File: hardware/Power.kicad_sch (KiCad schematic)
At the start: 36 parts

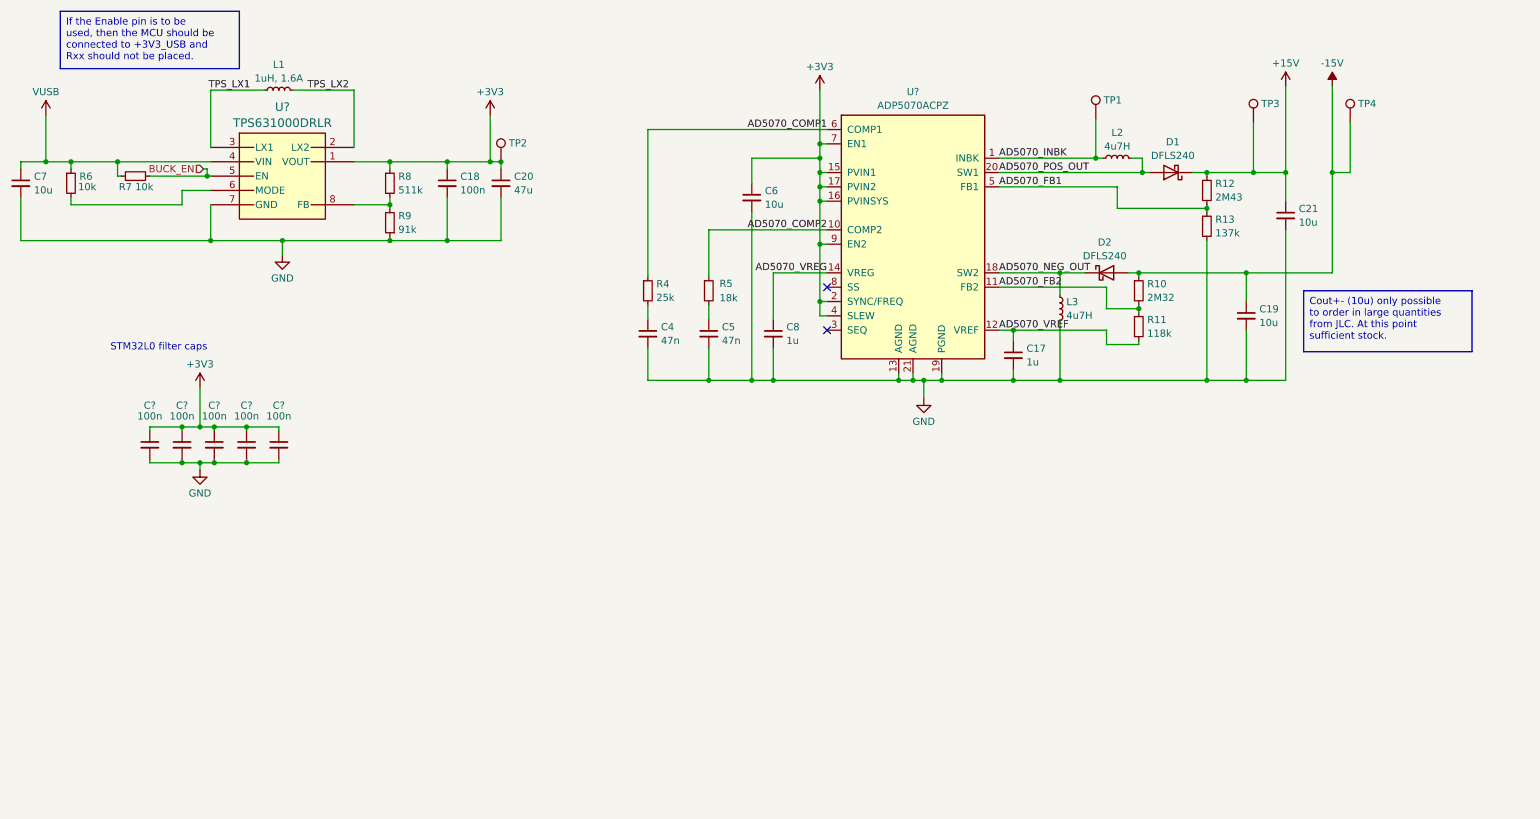
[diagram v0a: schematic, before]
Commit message: feat(RGB): WS2812B driver
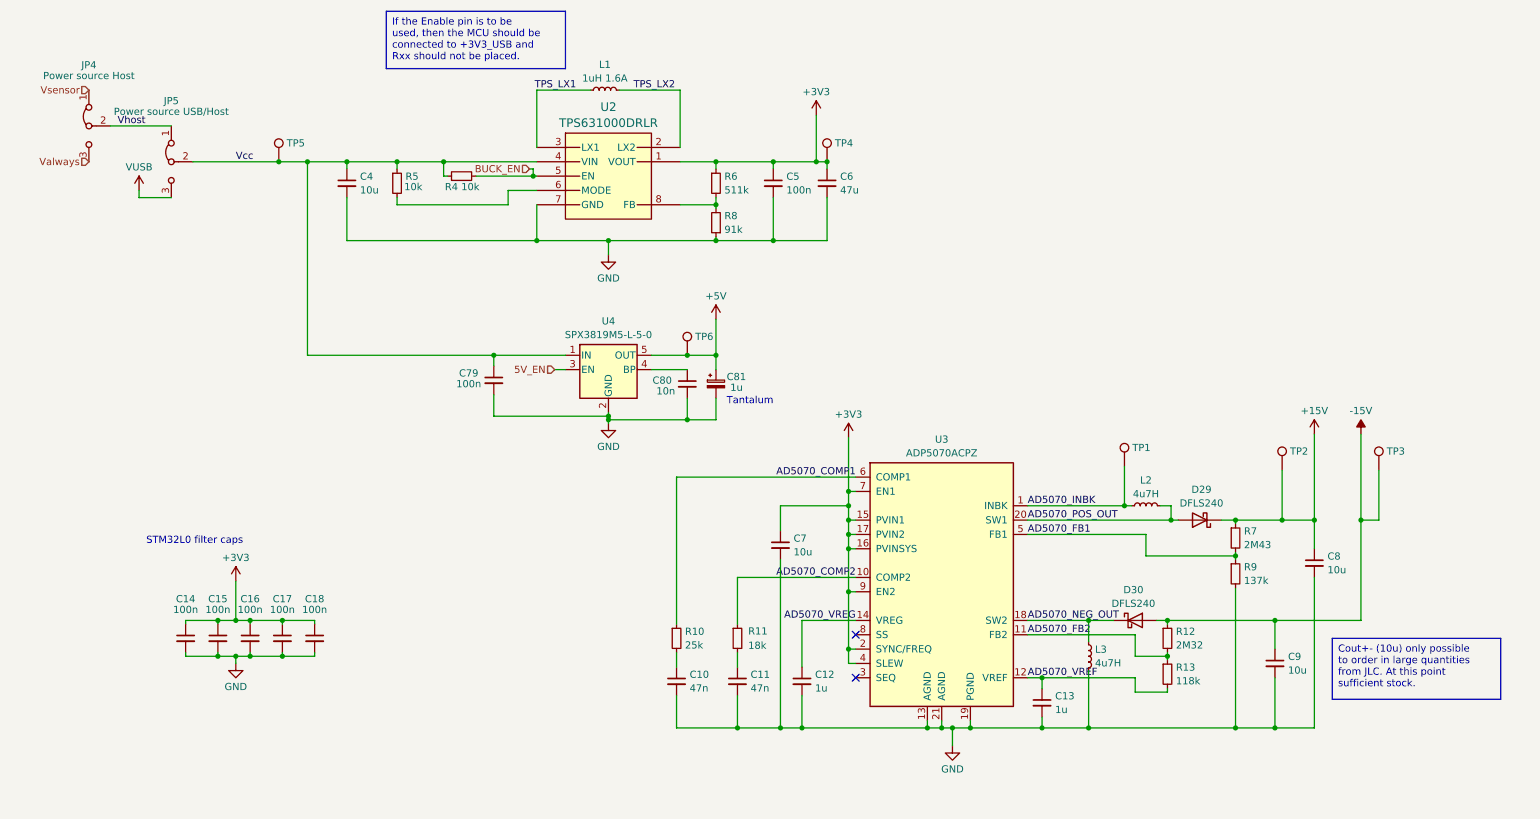
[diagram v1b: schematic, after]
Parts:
- added C79: 100n, Capacitor_SMD:C_0603_1608Metric, symbol Device:C_Small
- added C80: 10n, Capacitor_SMD:C_0603_1608Metric, symbol Device:C_Small
- added C81: 1u, Capacitor_Tantalum_SMD:CP_EIA-1608-08_AVX-J, symbol Device:C_Polarized_Small
- added JP4: Power source Host, Connector_PinHeader_2.54mm:PinHeader_1x03_P2.54mm_Vertical, symbol Jumper:Jumper_3_Bridged12
- added JP5: Power source USB/Host, Connector_PinHeader_2.54mm:PinHeader_1x03_P2.54mm_Vertical, symbol Jumper:Jumper_3_Bridged12
- added TP5, TP6: ~, TestPoint:TestPoint_Pad_D1.5mm, symbol Connector:TestPoint
- added U4: SPX3819M5-L-5-0, Package_TO_SOT_SMD:SOT-23-5, symbol Regulator_Linear:SPX3819M5-L-5-0
- L1: value 1uH, 1.6A -> 1uH 1.6A
- L2, L3: LCSC Part # (none) -> C9900037470
- gave numbers to parts that had none: 7
- renumbered C4 to C10, C5 to C11, C8 to C12, C17 to C13, C7 to C4, C18 to C5, C20 to C6, C6 to C7, C21 to C8, C19 to C9, D1 to D29, D2 to D30, R4 to R10, R5 to R11, R10 to R12, R11 to R13, R7 to R4, R6 to R5, R8 to R6, R12 to R7, R9 to R8, R13 to R9, TP3 to TP2, TP4 to TP3, TP2 to TP4
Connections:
- net GND: now also C79.2, C80.2, C81.2, U4.2 (GND)
- net VUSB: now also JP5.3 (B); no longer C4.1, R4.1, R5.1, U2.4 (VIN)
- new net: C80.1, U4.4 (BP)
- new net +5V: C81.1, TP6.1, U4.5 (OUT)
- new net 5V_EN: U4.3 (EN)
- new net Valways: JP4.3 (B)
- new net Vcc: C4.1, C79.1, JP5.2 (C), R4.1, R5.1, TP5.1, U2.4 (VIN), U4.1 (IN)
- new net Vhost: JP4.2 (C), JP5.1 (A)
- new net Vsensor: JP4.1 (A)
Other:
- note added: "Tantalum"
- moved on the sheet: C10, C11, C12, C13, C14, C15, C16, C17, C18, C4, C5, C6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

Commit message: HW: update to latest version
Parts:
- removed C14, C15, C16, C17, C18: 100n, Capacitor_SMD:C_0603_1608Metric, symbol Device:C_Small
- C81: footprint Capacitor_Tantalum_SMD:CP_EIA-1608-08_AVX-J -> custom_library_FP:CP-3216-18; LCSC MFR # 298D105X0025M2T -> 293D105X9025A2TE3; LCSC Part # C1952840 -> C511013
- R7: footprint Resistor_SMD:R_0603_1608Metric -> Resistor_SMD:R_0805_2012Metric; LCSC MFR # RC0603FR-072M43L -> RC0805FR-072M43L; LCSC Part # C482795 -> C483044
- U2: footprint TPS631000DRLR:TPS631000DRLR_TEX -> ul_TPS631000DRLR:TPS631000DRLR_TEX
- U3: symbol Regulator_Switching:ADP5070ACPZ -> custom_library:ADP5070ACPZ
- U4: LCSC MFR (none) -> MaxLinear; LCSC MFR # (none) -> SPX3819M5-L-5-0/TR; LCSC Part # (none) -> C13417
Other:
- note removed: "STM32L0 filter caps"
- company: Avalution Engineering -> Avalution Engineering / Pollex
- title: Zoutwachter Switch -> Zoutwachter Measurement-Switch
- moved on the sheet: C10, C11, C12, C13, C4, C6, C7, C79, C8, D29, D30, JP4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
